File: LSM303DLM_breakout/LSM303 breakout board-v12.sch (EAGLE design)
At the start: 20 parts, among them Q1 MOSFET-N-CH, Q2 MOSFET-N-CH, U1 LSM303DLHSMD, U2 1.8V, U3 3.3V

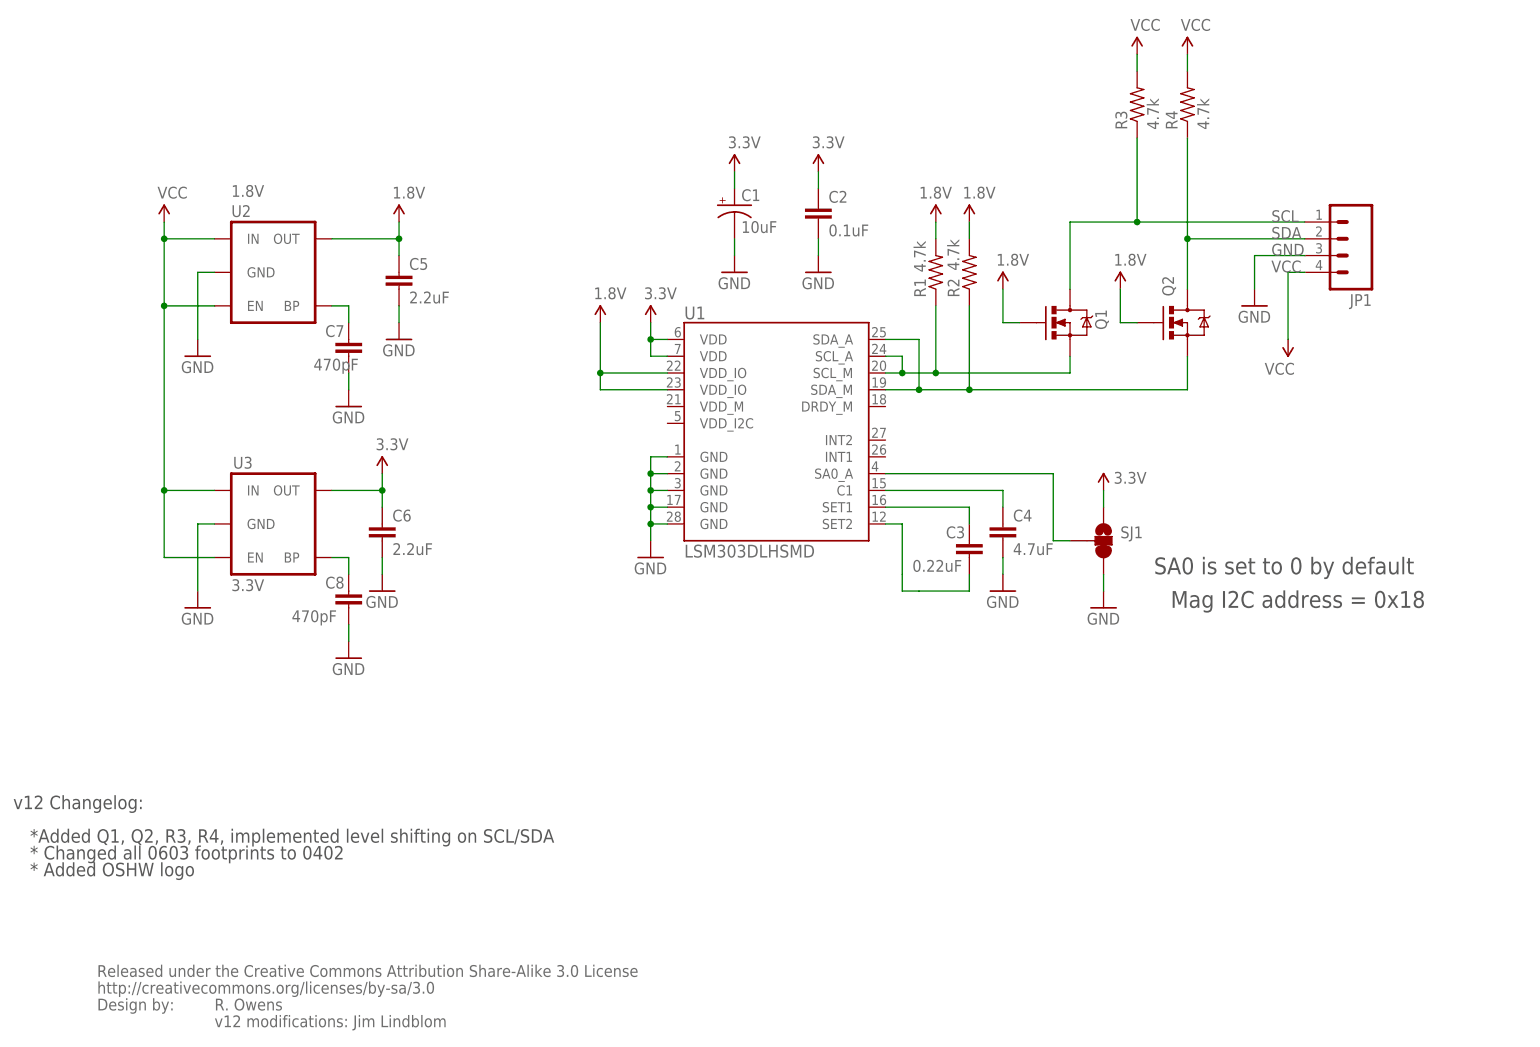
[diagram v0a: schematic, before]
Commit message: Version 0.2. Make board a lot simpler.
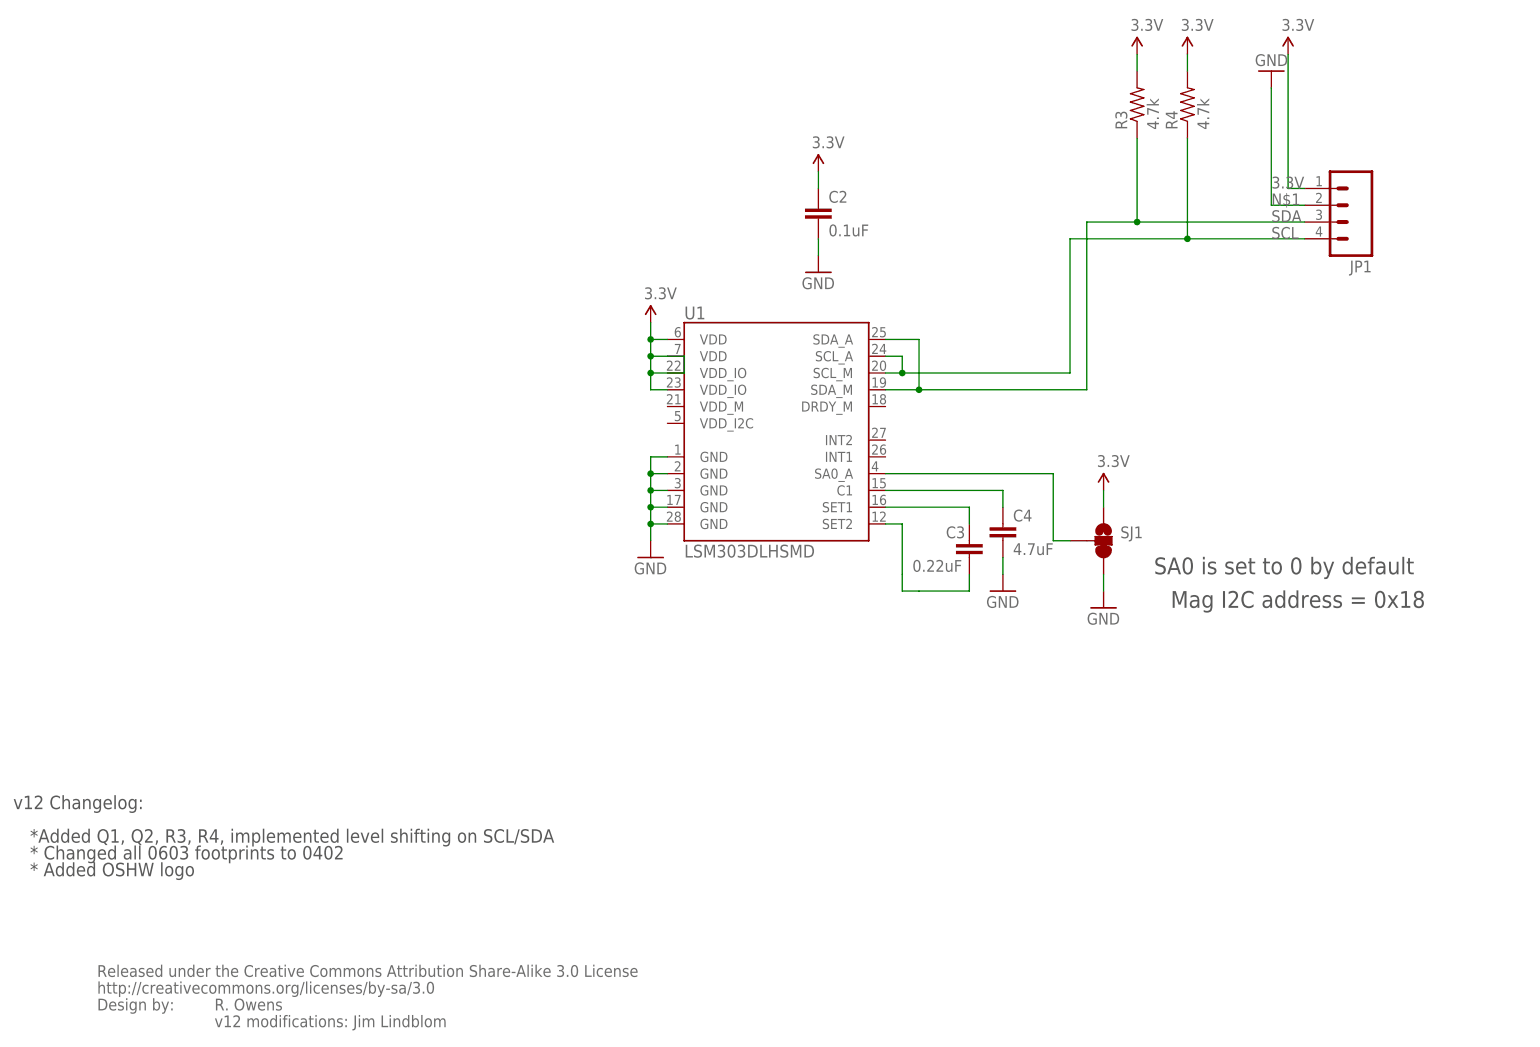
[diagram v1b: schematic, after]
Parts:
- removed C1: 10uF, SparkFun:CAP_POL1206
- removed C5, C6: 2.2uF, SparkFun:CAP0402-CAP
- removed C7, C8: 470pF, SparkFun:CAP0402-CAP
- removed Q1, Q2: MOSFET-N-CH, SparkFun:MOSFET-NCHANNELSMD
- removed R1, R2: 4.7k, SparkFun:RESISTOR0805-RES
- removed U2: 1.8V, SparkFun:V_REG_LDOSMD2
- removed U3: 3.3V, SparkFun:V_REG_LDOSMD
- C2, C3: device SparkFun:CAP0402-CAP -> SparkFun:CAP0603-CAP
- C4: device SparkFun:CAP0402-CAP -> SparkFun:CAP1206
- JP1: device SparkFun:M04PTH -> SparkFun-Connectors:M04PTH
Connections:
- removed net 1.8V: C5.1, Q1.G, Q2.G, R1.2, R2.2, U1.VDD_IO@22, U1.VDD_IO@23, U2.OUT
- removed net GND: C1.-, C2.2, C4.2, C5.2, C6.2, C7.2, C8.2, JP1.3, SJ1.3, U1.GND@1, U1.GND@17, U1.GND@2, U1.GND@28, U1.GND@3, U2.GND, U3.GND
- removed net N$6: C7.1, U2.BP
- removed net N$7: C8.1, U3.BP
- removed net SCL_M: Q1.S, R1.1, U1.SCL_A, U1.SCL_M
- removed net SDA_M: Q2.S, R2.1, U1.SDA_A, U1.SDA_M
- removed net VCC: JP1.4, R3.2, R4.2, U2.EN, U2.IN, U3.EN, U3.IN
- new net N$1: C2.2, C4.2, JP1.2, SJ1.3, U1.GND@1, U1.GND@17, U1.GND@2, U1.GND@28, U1.GND@3
- net 3.3V: now also JP1.1, R3.2, R4.2, U1.VDD_IO@23; no longer C1.+, C6.1, U3.OUT
- net SCL: now also JP1.4, R4.1, U1.SCL_A, U1.SCL_M; no longer JP1.1, Q1.D, R3.1
- net SDA: now also JP1.3, R3.1, U1.SDA_A, U1.SDA_M; no longer JP1.2, Q2.D, R4.1
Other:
- moved on the sheet: JP1

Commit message: Minor modifications.
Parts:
- R3, R4: device SparkFun:RESISTOR0805-RES -> SparkFun:RESISTOR0603-RES
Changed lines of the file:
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@@
 <part name="GND3" library="SparkFun" deviceset="GND" device=""/>
 <part name="U$5" library="SparkFun" deviceset="CREATIVE_COMMONS" device=""/>
-<part name="R3" library="SparkFun" deviceset="RESISTOR" device="0805-RES" value="4.7k"/>
-<part name="R4" library="SparkFun" deviceset="RESISTOR" device="0805-RES" value="4.7k"/>
+<part name="R3" library="SparkFun" deviceset="RESISTOR" device="0603-RES" value="4.7k"/>
+<part name="R4" library="SparkFun" deviceset="RESISTOR" device="0603-RES" value="4.7k"/>
 <part name="P+3" library="SparkFun-Aesthetics" deviceset="3.3V" device=""/>
 <part name="P+6" library="SparkFun-Aesthetics" deviceset="3.3V" device=""/>
